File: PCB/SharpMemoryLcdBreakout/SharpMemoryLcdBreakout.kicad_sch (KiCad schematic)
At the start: 10 parts, among them J1 Pin Header, J2 EMD, J3 FH12-10S-0.5SH

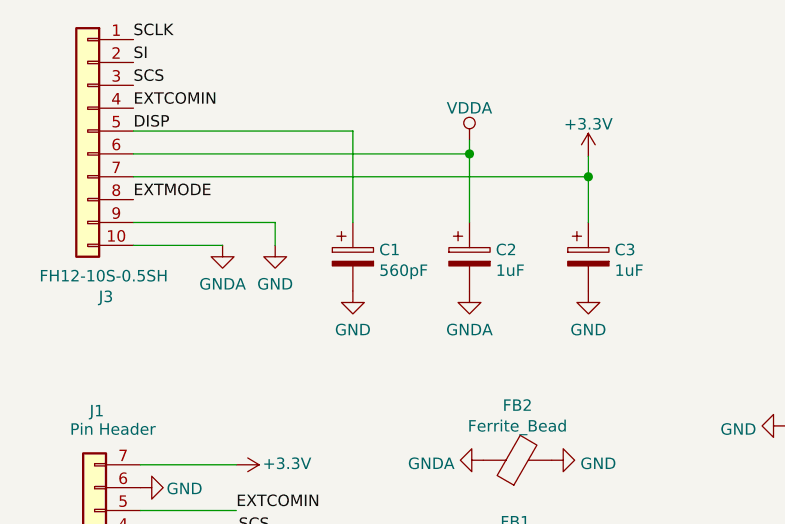
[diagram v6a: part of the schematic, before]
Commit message: going back to 0603 for easier part selection
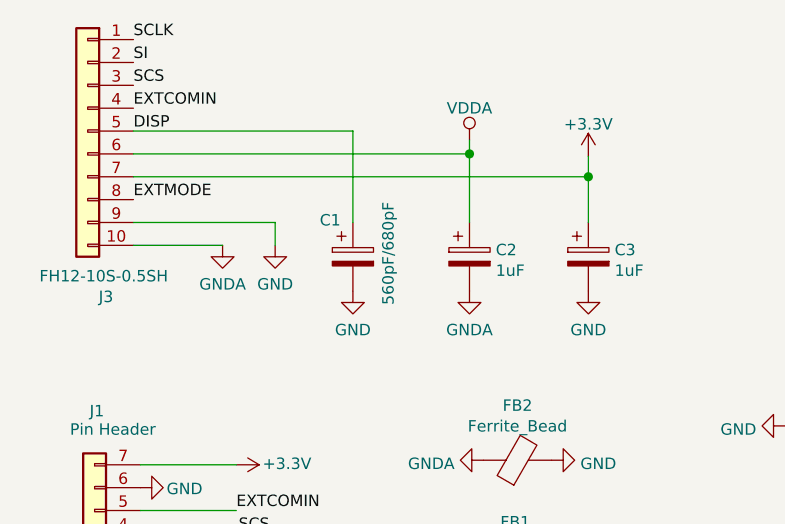
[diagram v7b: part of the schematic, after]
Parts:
- C1: value 560pF -> 560pF/680pF; footprint Capacitor_SMD:C_0805_2012Metric_Pad1.15x1.40mm_HandSolder -> Capacitor_SMD:C_0603_1608Metric_Pad1.05x0.95mm_HandSolder; LCSC C107119 -> C1630
- C2, C3: footprint Capacitor_SMD:C_0805_2012Metric_Pad1.15x1.40mm_HandSolder -> Capacitor_SMD:C_0603_1608Metric_Pad1.05x0.95mm_HandSolder; LCSC C28323 -> C15849
- R1, R2: footprint Resistor_SMD:R_0805_2012Metric_Pad1.15x1.40mm_HandSolder -> Resistor_SMD:R_0603_1608Metric_Pad1.05x0.95mm_HandSolder; LCSC C365230 -> C25804
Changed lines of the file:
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@@
     (property "Reference" "R1" (id 0) (at 111.252 62.8862 90))
     (property "Value" "10kΩ" (id 1) (at 111.252 65.1849 90))
-    (property "Footprint" "Resistor_SMD:R_0805_2012Metric_Pad1.15x1.40mm_HandSolder" (id 2) (at 111.252 67.056 0)
+    (property "Footprint" "Resistor_SMD:R_0603_1608Metric_Pad1.05x0.95mm_HandSolder" (id 2) (at 111.252 67.056 0)
       (effects (font (size 1.27 1.27)) hide)
     )
@@
       (effects (font (size 1.27 1.27)) hide)
     )
-    (property "LCSC" "C365230" (id 4) (at 111.252 67.056 90)
+    (property "LCSC" "C25804" (id 4) (at 111.252 67.056 90)
       (effects (font (size 1.27 1.27)) hide)
     )
@@
     (property "Reference" "R2" (id 0) (at 119.888 62.8862 90))
     (property "Value" "10kΩ" (id 1) (at 119.888 65.1849 90))
-    (property "Footprint" "Resistor_SMD:R_0805_2012Metric_Pad1.15x1.40mm_HandSolder" (id 2) (at 119.888 67.056 0)
+    (property "Footprint" "Resistor_SMD:R_0603_1608Metric_Pad1.05x0.95mm_HandSolder" (id 2) (at 119.888 67.056 0)
       (effects (font (size 1.27 1.27)) hide)
     )
@@
       (effects (font (size 1.27 1.27)) hide)
     )
-    (property "LCSC" "C365230" (id 4) (at 119.888 67.056 90)
+    (property "LCSC" "C25804" (id 4) (at 119.888 67.056 90)
       (effects (font (size 1.27 1.27)) hide)
     )
@@
   )
   (symbol (lib_id "Device:CP") (at 60.706 48.26 0) (unit 1)
-    (in_bom yes) (on_board yes) (fields_autoplaced)
-    (property "Reference" "C1" (id 0) (at 63.6271 47.4991 0)
-      (effects (font (size 1.27 1.27)) (justify left))
-    )
-    (property "Value" "560pF" (id 1) (at 63.6271 49.7978 0)
-      (effects (font (size 1.27 1.27)) (justify left))
-    )
-    (property "Footprint" "Capacitor_SMD:C_0805_2012Metric_Pad1.15x1.40mm_HandSolder" (id 2) (at 61.6712 52.07 0)
+    (in_bom yes) (on_board yes)
+    (property "Reference" "C1" (id 0) (at 57.0231 44.1971 0)
+      (effects (font (size 1.27 1.27)) (justify left))
+    )
+    (property "Value" "560pF/680pF" (id 1) (at 64.6431 53.6078 90)
+      (effects (font (size 1.27 1.27)) (justify left))
+    )
+    (property "Footprint" "Capacitor_SMD:C_0603_1608Metric_Pad1.05x0.95mm_HandSolder" (id 2) (at 61.6712 52.07 0)
       (effects (font (size 1.27 1.27)) hide)
     )
@@
       (effects (font (size 1.27 1.27)) hide)
     )
-    (property "LCSC" "C107119" (id 4) (at 60.706 48.26 0)
+    (property "LCSC" "C1630" (id 4) (at 60.706 48.26 0)
       (effects (font (size 1.27 1.27)) hide)
     )
@@
       (effects (font (size 1.27 1.27)) (justify left))
     )
-    (property "Footprint" "Capacitor_SMD:C_0805_2012Metric_Pad1.15x1.40mm_HandSolder" (id 2) (at 74.6252 52.07 0)
+    (property "Footprint" "Capacitor_SMD:C_0603_1608Metric_Pad1.05x0.95mm_HandSolder" (id 2) (at 74.6252 52.07 0)
       (effects (font (size 1.27 1.27)) hide)
     )
@@
       (effects (font (size 1.27 1.27)) hide)
     )
-    (property "LCSC" "C28323" (id 4) (at 73.66 48.26 0)
+    (property "LCSC" "C15849" (id 4) (at 73.66 48.26 0)
       (effects (font (size 1.27 1.27)) hide)
     )
@@
       (effects (font (size 1.27 1.27)) (justify left))
     )
-    (property "Footprint" "Capacitor_SMD:C_0805_2012Metric_Pad1.15x1.40mm_HandSolder" (id 2) (at 87.8332 52.07 0)
+    (property "Footprint" "Capacitor_SMD:C_0603_1608Metric_Pad1.05x0.95mm_HandSolder" (id 2) (at 87.8332 52.07 0)
       (effects (font (size 1.27 1.27)) hide)
     )
@@
       (effects (font (size 1.27 1.27)) hide)
     )
-    (property "LCSC" "C28323" (id 4) (at 86.868 48.26 0)
+    (property "LCSC" "C15849" (id 4) (at 86.868 48.26 0)
       (effects (font (size 1.27 1.27)) hide)
     )
@@
     )
     (path "/7a602df9-b4ab-4c8f-bcee-115ea78044b1"
-      (reference "C1") (unit 1) (value "560pF") (footprint "Capacitor_SMD:C_0805_2012Metric_Pad1.15x1.40mm_HandSolder")
+      (reference "C1") (unit 1) (value "560pF/680pF") (footprint "Capacitor_SMD:C_0603_1608Metric_Pad1.05x0.95mm_HandSolder")
     )
     (path "/83e00d4f-b880-41eb-a80c-47548e30c913"
-      (reference "C2") (unit 1) (value "1uF") (footprint "Capacitor_SMD:C_0805_2012Metric_Pad1.15x1.40mm_HandSolder")
+      (reference "C2") (unit 1) (value "1uF") (footprint "Capacitor_SMD:C_0603_1608Metric_Pad1.05x0.95mm_HandSolder")
     )
     (path "/d11b5518-01e5-473f-a82d-fa89aa1fe8d7"
-      (reference "C3") (unit 1) (value "1uF") (footprint "Capacitor_SMD:C_0805_2012Metric_Pad1.15x1.40mm_HandSolder")
+      (reference "C3") (unit 1) (value "1uF") (footprint "Capacitor_SMD:C_0603_1608Metric_Pad1.05x0.95mm_HandSolder")
     )
     (path "/89deffba-7955-40a3-9fd3-26677edd0547"
@@
     )
     (path "/26fa69b4-96a4-485c-8f3c-4f68027d84ab"
-      (reference "R1") (unit 1) (value "10kΩ") (footprint "Resistor_SMD:R_0805_2012Metric_Pad1.15x1.40mm_HandSolder")
+      (reference "R1") (unit 1) (value "10kΩ") (footprint "Resistor_SMD:R_0603_1608Metric_Pad1.05x0.95mm_HandSolder")
     )
     (path "/73050aba-79d3-41c7-b66e-cd8669eda61f"
-      (reference "R2") (unit 1) (value "10kΩ") (footprint "Resistor_SMD:R_0805_2012Metric_Pad1.15x1.40mm_HandSolder")
-    )
-  )
+      (reference "R2") (unit 1) (value "10kΩ") (footprint "Resistor_SMD:R_0603_1608Metric_Pad1.05x0.95mm_HandSolder")
+    )
+  )
